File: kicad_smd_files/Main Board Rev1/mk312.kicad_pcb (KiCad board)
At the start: 4 copper layers, 135 x 83.5 mm, 171 parts, among them IC1 LD1086BDTTR, IC2 L7805CV, IC3 L7809ABV, IC4 L7809ABV, J1 Barrel_Jack_MountingPin, J10 OUTPUT B, J11 Conn_01x24_Male, J12 Conn_01x24_Male, J2 +12V Battery, J3 Conn_02x03_Odd_Even, J4 RADIO INTERFACE, J5 MIC INPUT, J6 LINE INPUT, J7 REMOTE INPUT, J8 LINK INPUT, J9 OUTPUT A, Q1 MMBT3904-7-F, Q2 MMBT3904-7-F, Q3 DMN10H170SK3-13, Q4 DMP6180SK3-13, Q5 DMN10H170SK3-13, Q6 DMN10H170SK3-13, Q7 DMP6180SK3-13, Q8 DMN10H170SK3-13, SW2 LEFT/DOWN, SW3 OK, SW4 RIGHT/UP, SW5 MENU, U1 ATmega16-16AU, U2 MCP6L01U, U3 CD4006B, U4 SP232E, U6 LM324N, U7 LM358N, U8 LTC1661

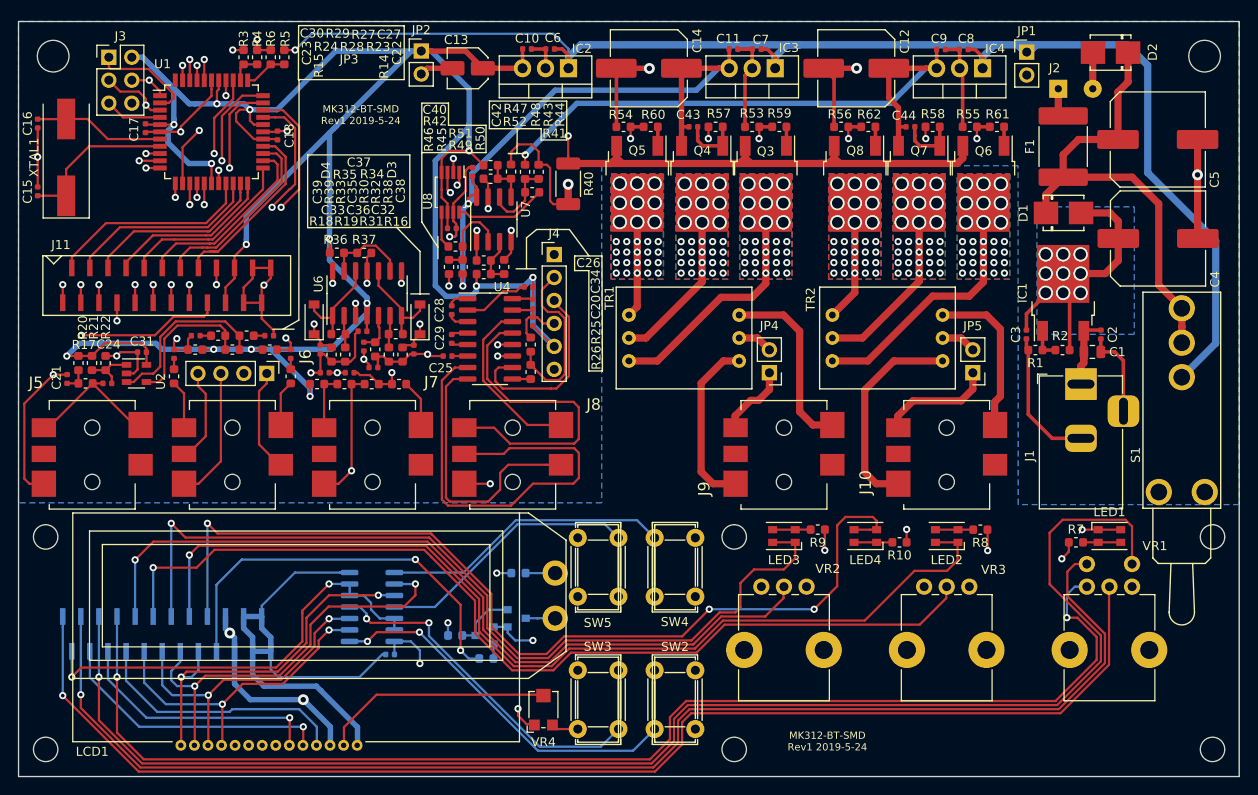
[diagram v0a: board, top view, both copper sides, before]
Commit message: Firmware patch to support new LCD, more beefy power circuit for LiPo, added LiPo Balance and protection, fixed reversed op-amp comparitor pins
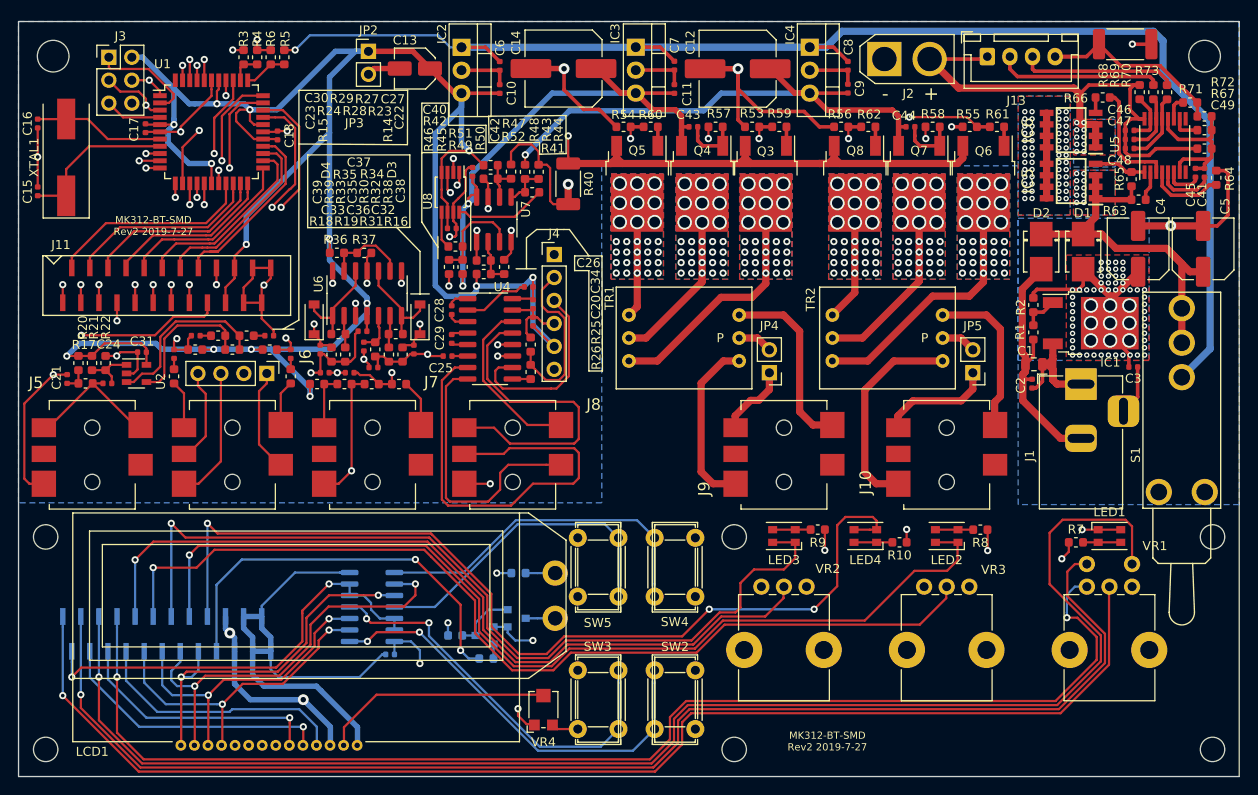
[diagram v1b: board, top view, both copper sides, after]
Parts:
- removed F1: 1A Polyfuse, Fuse:Fuse_2920_7451Metric
- removed JP1: +12V, Connector_PinHeader_2.54mm:PinHeader_1x02_P2.54mm_Vertical
- added C41: 0.1uF, Capacitor_SMD:C_0402_1005Metric, F.Cu at (206.8, 39.2)
- added C45: 0.1uF, Capacitor_SMD:C_0402_1005Metric, F.Cu at (205.8, 39.2)
- added C46: 0.1uF, Capacitor_SMD:C_0402_1005Metric, F.Cu at (198.5, 34.5)
- added C47: 0.1uF, Capacitor_SMD:C_0402_1005Metric, F.Cu at (198.5, 35.5)
- added C48: 0.1uF, Capacitor_SMD:C_0402_1005Metric, F.Cu at (198.5, 36.5)
- added C49: 2.2uF, Capacitor_SMD:C_0603_1608Metric, F.Cu at (206.8, 36.6)
- added IC5: SI4435FDY-T1-GE3, mk312-smd-footprints:SOIC127P600X175-8N, F.Cu at (192.0, 40.1)
- added IC6: SI4435FDY-T1-GE3, mk312-smd-footprints:SOIC127P600X175-8N, F.Cu at (192.0, 34.5)
- added J13: Conn_01x04, Connector_JST:JST_XH_B4B-XH-A_1x04_P2.50mm_Vertical, F.Cu at (182.7, 26.4)
- added R63: 5.1K, Resistor_SMD:R_0603_1608Metric, F.Cu at (199.5, 42.2)
- added R64: 1K, Resistor_SMD:R_0603_1608Metric, F.Cu at (208.1, 39.8)
- added R65: 1M, Resistor_SMD:R_0603_1608Metric, F.Cu at (198.7, 39.9)
- added R66: 5.1K, Resistor_SMD:R_0603_1608Metric, F.Cu at (195.5, 30.9)
- added R67: 1K, Resistor_SMD:R_0603_1608Metric, F.Cu at (206.8, 34.5)
- added R68: 1K, Resistor_SMD:R_0603_1608Metric, F.Cu at (199.6, 30.3)
- added R69: 1K, Resistor_SMD:R_0603_1608Metric, F.Cu at (201.1, 30.3)
- added R70: 1K, Resistor_SMD:R_0603_1608Metric, F.Cu at (202.6, 30.3)
- added R71: 1K, Resistor_SMD:R_0603_1608Metric, F.Cu at (205.2, 31.5)
- added R72: 51, Resistor_SMD:R_0603_1608Metric, F.Cu at (206.8, 33.0)
- added R73: 0.2R 2W, Resistor_SMD:R_2512_6332Metric, F.Cu at (198.0, 25.0)
- added U5: S-8254A, Package_SO:TSSOP-16_4.4x5mm_P0.65mm, F.Cu at (202.4, 36.2)
- C4, C5: value 1000uF -> 100uF; footprint Capacitor_SMD:C_Elec_10x10.2 -> Capacitor_SMD:C_Elec_6.3x7.7
- IC1: value LD1086BDTTR -> LMS8117ADTX-ADJ
- J2: footprint Connector_Wire:SolderWirePad_1x02_P3.81mm_Drill0.8mm -> Connector_AMASS:AMASS_XT30U-M_1x02_P5.0mm_Vertical
- Q3, Q5, Q6, Q8: value DMN10H170SK3-13 -> IRFR9024NTRPBF
- Q4, Q7: value DMP6180SK3-13 -> IRLR120NTRPBF
- R11: value 47 -> 130
- U3: value CD4006B -> CD4066B
- moved D2 23.3 mm to (188.7, 48.0), turned to 270 degrees
- moved J2 19.5 mm to (171.4, 26.6)
- moved IC4 19.3 mm to (163.1, 25.3), turned to 270 degrees
- moved IC3 15.6 mm to (143.9, 25.3), turned to 270 degrees
- moved C12 13.1 mm to (155.1, 27.7)
- moved C5 13.1 mm to (206.6, 47.6), turned to 90 degrees
- moved C8 12.9 mm to (167.3, 27.4), turned to 270 degrees
- moved C3 12.3 mm to (198.9, 60.7), turned to 0 degrees
- moved IC2 12.1 mm to (124.6, 25.4), turned to 270 degrees
- moved C9 11.2 mm to (167.3, 29.9), turned to 90 degrees
- moved C14 9.44 mm to (135.9, 27.7)
- moved C2 9.35 mm to (187.7, 62.5), turned to 90 degrees
- moved C7 9.29 mm to (148.1, 27.4), turned to 270 degrees
- moved C11 7.87 mm to (148.1, 30.0), turned to 90 degrees
- moved C1 6.60 mm to (187.9, 60.4), turned to 180 degrees
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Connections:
- J2 pad 1: Net-(F1-Pad2) -> GND
- J2 pad 2: GND -> Net-(C46-Pad1)
- U7 pad 2: Net-(R42-Pad1) -> Net-(R49-Pad2)
- U7 pad 3: Net-(R49-Pad2) -> Net-(R42-Pad1)
- U7 pad 5: Net-(R47-Pad2) -> Net-(R41-Pad1)
- U7 pad 6: Net-(R41-Pad1) -> Net-(R47-Pad2)
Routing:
- net Net-(C46-Pad1): track 0.00 -> 58.1 mm, vias 0 -> 10
- net GND: track 250.0 -> 276.0 mm, vias 20 -> 22
- net Net-(J13-Pad4): track 0.00 -> 22.3 mm
- net +VDC: track 139.1 -> 161.4 mm
- net Net-(J13-Pad2): track 0.00 -> 18.3 mm
- net Net-(C41-Pad2): track 0.00 -> 18.0 mm
- net Net-(J13-Pad3): track 0.00 -> 17.3 mm
- net Net-(R66-Pad2): track 0.00 -> 12.6 mm
- net +5V: track 282.0 -> 271.5 mm
- net Net-(IC5-Pad5): track 0.00 -> 9.44 mm, vias 0 -> 52
- net Net-(C5-Pad1): track 52.3 -> 43.2 mm, vias 0 -> 10
- net Net-(R64-Pad2): track 0.00 -> 8.42 mm
- net +9V1: track 70.2 -> 62.0 mm
- net +12V: track 162.8 -> 154.9 mm
- net Net-(C48-Pad2): track 0.00 -> 7.74 mm
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- added copper zone on F.Cu, net Net-(C3-Pad1)
- added copper zone on B.Cu, net Net-(C46-Pad1)
- added copper zone on F.Cu, net Net-(C46-Pad1)
- added copper zone on B.Cu, net Net-(C5-Pad1)
- added copper zone on F.Cu, net Net-(C5-Pad1)
- added copper zone on B.Cu, net Net-(IC5-Pad5)
- added copper zone on F.Cu, net Net-(IC5-Pad5)
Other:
- board text added: "MK312-BT-SMD Rev2 2019-7-27"
- board text added: "P"
- board text removed: "MK312-BT-SMD Rev1 2019-5-24"
